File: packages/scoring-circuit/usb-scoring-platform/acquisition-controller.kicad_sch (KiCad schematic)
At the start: 17 parts, among them J2 STM SWD 3.3V, SW1 STM RESET, U1 STM32G474RET6, Y1 ABM3B-8.000MHZ-B2-T

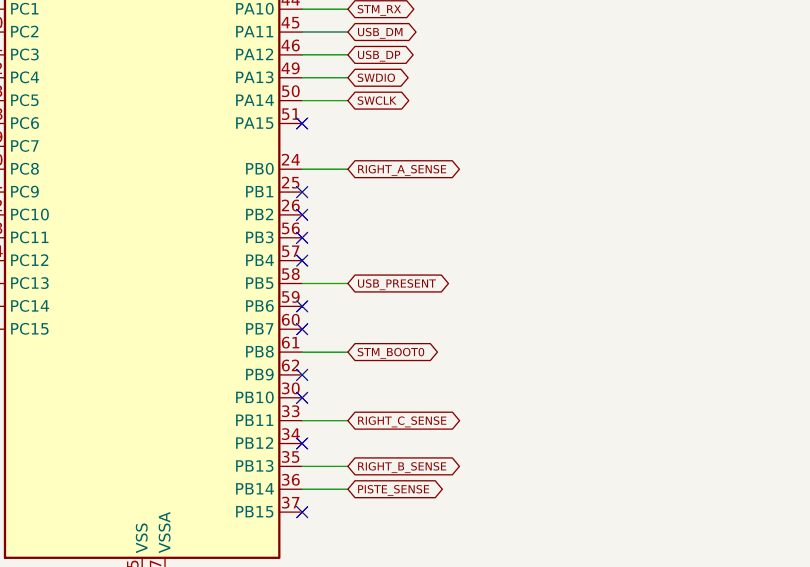
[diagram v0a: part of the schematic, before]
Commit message: feat(scoring-circuit): isolate computer USB in native KiCad draft
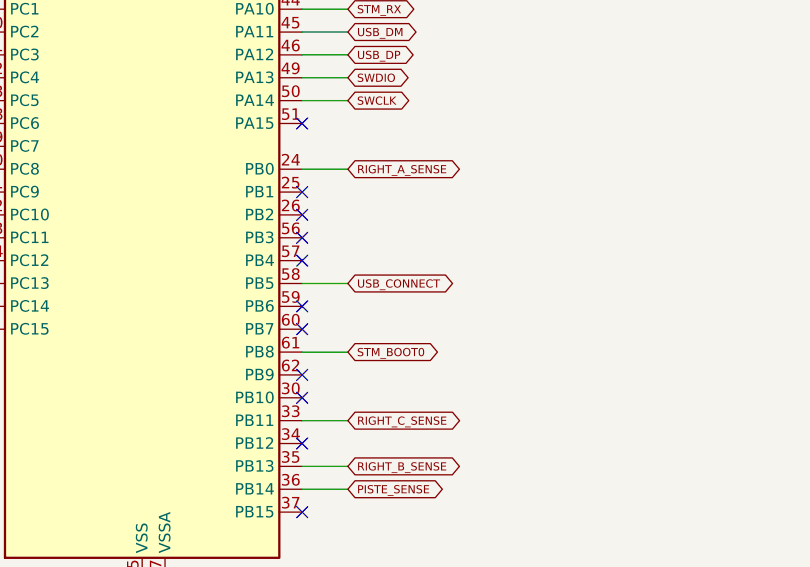
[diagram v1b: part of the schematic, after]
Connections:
- net USB_PRESENT renamed USB_CONNECT

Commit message: feat(scoring-circuit): add isolated single-cable USB acquisition power
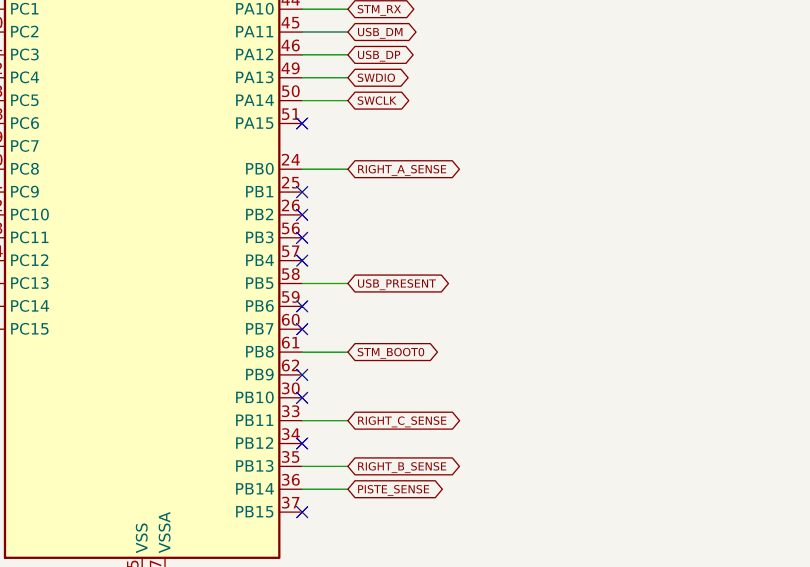
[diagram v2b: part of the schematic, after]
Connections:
- net USB_CONNECT renamed USB_PRESENT
